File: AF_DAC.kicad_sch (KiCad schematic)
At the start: 27 parts, among them J9 3.5mm_Jack, U12 PAM8908, U4 CJC4334H

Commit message: Fixed a lot more mistakes...
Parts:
- TP8, TP9: footprint TP_Label:TestPoint_THTPad_D2.0mm_Drill1.0mm -> TestPoint:TestPoint_THTPad_D2.5mm_Drill1.2mm
- U12: Price (none) -> $0.38
- U4: Price (none) -> $0.30
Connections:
- net +3.3V renamed +3V3
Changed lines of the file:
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@@
 			)
 		)
-		(property "Footprint" "TP_Label:TestPoint_THTPad_D2.0mm_Drill1.0mm"
+		(property "Footprint" "TestPoint:TestPoint_THTPad_D2.5mm_Drill1.2mm"
 			(at 212.09 96.52 0)
 			(hide yes)
@@
 			)
 		)
+		(property "Price" "$0.38"
+			(at 166.37 88.9 0)
+			(hide yes)
+			(show_name no)
+			(do_not_autoplace no)
+			(effects
+				(font
+					(size 1.27 1.27)
+				)
+			)
+		)
 		(pin "2"
 		)
@@
 	)
 	(symbol
+		(lib_id "power:+3V3")
+		(at 72.39 53.34 0)
+		(unit 1)
+		(body_style 1)
+		(exclude_from_sim no)
+		(in_bom yes)
+		(on_board yes)
+		(in_pos_files yes)
+		(dnp no)
+		(property "Reference" "#PWR0220"
+			(at 72.39 57.15 0)
+			(hide yes)
+			(show_name no)
+			(do_not_autoplace no)
+			(effects
+				(font
+					(size 1.27 1.27)
+				)
+			)
+		)
+		(property "Value" "+3V3"
+			(at 72.771 48.9458 0)
+			(show_name no)
+			(do_not_autoplace no)
+			(effects
+				(font
+					(size 1.27 1.27)
+				)
+			)
+		)
+		(property "Footprint" ""
+			(at 72.39 53.34 0)
+			(hide yes)
+			(show_name no)
+			(do_not_autoplace no)
+			(effects
+				(font
+					(size 1.27 1.27)
+				)
+			)
+		)
+		(property "Datasheet" ""
+			(at 72.39 53.34 0)
+			(hide yes)
+			(show_name no)
+			(do_not_autoplace no)
+			(effects
+				(font
+					(size 1.27 1.27)
+				)
+			)
+		)
+		(property "Description" ""
+			(at 72.39 53.34 0)
+			(hide yes)
+			(show_name no)
+			(do_not_autoplace no)
+			(effects
+				(font
+					(size 1.27 1.27)
+				)
+			)
+		)
+		(pin "1"
+		)
+		(instances
+			(project "DDC_SDR"
+				(path "/7dfef218-ca21-47b0-a8d3-67c7d55cb9d2/41fc8a82-80f7-4b0c-8115-38fd99a62892"
+					(reference "#PWR0220")
+					(unit 1)
+				)
+			)
+		)
+	)
+	(symbol
 		(lib_id "power:GNDA")
 		(at 72.39 102.87 0)
@@
 			)
 		)
-		(property "Footprint" "TP_Label:TestPoint_THTPad_D2.0mm_Drill1.0mm"
+		(property "Footprint" "TestPoint:TestPoint_THTPad_D2.5mm_Drill1.2mm"
 			(at 222.25 86.36 0)
 			(hide yes)
@@
 			)
 		)
+		(property "Price" "$0.30"
+			(at 71.12 87.63 0)
+			(hide yes)
+			(show_name no)
+			(do_not_autoplace no)
+			(effects
+				(font
+					(size 1.27 1.27)
+				)
+			)
+		)
 		(pin "2"
 		)
@@
 					(unit 1)
 				)
-			)
-		)
-	)
-	(symbol
-		(lib_name "+3.3V_1")
-		(lib_id "power:+3.3V")
-		(at 72.39 53.34 0)
-		(mirror y)
-		(unit 1)
-		(body_style 1)
-		(exclude_from_sim no)
-		(in_bom yes)
-		(on_board yes)
-		(in_pos_files yes)
-		(dnp no)
-		(fields_autoplaced yes)
-		(property "Reference" "#PWR072"
-			(at 72.39 57.15 0)
-			(hide yes)
-			(show_name no)
-			(do_not_autoplace no)
-			(effects
-				(font
-					(size 1.27 1.27)
-				)
-			)
-		)
-		(property "Value" "+3.3V"
-			(at 72.39 48.26 0)
-			(show_name no)
-			(do_not_autoplace no)
-			(effects
-				(font
-					(size 1.27 1.27)
-				)
-			)
-		)
-		(property "Footprint" ""
-			(at 72.39 53.34 0)
-			(hide yes)
-			(show_name no)
-			(do_not_autoplace no)
-			(effects
-				(font
-					(size 1.27 1.27)
-				)
-			)
-		)
-		(property "Datasheet" ""
-			(at 72.39 53.34 0)
-			(hide yes)
-			(show_name no)
-			(do_not_autoplace no)
-			(effects
-				(font
-					(size 1.27 1.27)
-				)
-			)
-		)
-		(property "Description" "Power symbol creates a global label with name \"+3.3V\""
-			(at 72.39 53.34 0)
-			(hide yes)
-			(show_name no)
-			(do_not_autoplace no)
-			(effects
-				(font
-					(size 1.27 1.27)
-				)
-			)
-		)
-		(pin "1"
-		)
-		(instances
-			(project "DDC_SDR"
-				(path "/7dfef218-ca21-47b0-a8d3-67c7d55cb9d2/41fc8a82-80f7-4b0c-8115-38fd99a62892"
-					(reference "#PWR072")
-					(unit 1)
-				)

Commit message: Starting to place components
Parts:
- C12, C50: footprint PCM_JLCPCB:C_0805 -> PCM_JLCPCB:C_0402; symbol PCM_JLCPCB-Capacitors:0805,100nF -> PCM_JLCPCB-Capacitors:0402,100nF,(2); LCSC C28233 -> C307331; Manufacturer (none) -> Samsung Electro-Mechanics; Part CL21B104KCFNNNE -> CL05B104KB54PNC; Price 0.009USD -> 0.008USD; Stock 1168020 -> 8389599; Voltage Rated 100V -> 50V
- C26, C57: footprint PCM_JLCPCB:C_0805 -> PCM_JLCPCB:C_0603; symbol PCM_JLCPCB-Capacitors:0805,1uF -> PCM_JLCPCB-Capacitors:0603,1uF; LCSC C28323 -> C15849; Part CL21B105KBFNNNE -> CL10A105KB8NNNC; Price 0.012USD -> 0.008USD; Stock 4334256 -> 11535980; Temperature Coefficient X7R -> X5R
- C45: footprint PCM_JLCPCB:C_CASE-A-3216-18(mm) -> PCM_JLCPCB:C_0805; symbol PCM_JLCPCB-Capacitors:CASE-A-3216-18(mm),10uF -> PCM_JLCPCB-Capacitors:0805,10uF,(2); Attrition Qty 2 -> 4; Category Capacitors,Tantalum Capacitors -> Capacitors,Multilayer Ceramic Capacitors MLCC - SMD/SMT; LCSC C7171 -> C440198; Manufacturer (none) -> Murata Electronics; Part TAJA106K016RNJ -> GRM21BR61H106KE43L; Price 0.133USD -> 0.066USD; Stock 887054 -> 1422246; Temperature Coefficient (none) -> X5R; Voltage Rated (none) -> 50V
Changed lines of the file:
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@@
 	)
 	(symbol
-		(lib_id "PCM_JLCPCB-Capacitors:0805,1uF")
+		(lib_id "PCM_JLCPCB-Capacitors:0603,1uF")
 		(at 200.66 107.95 0)
 		(unit 1)
@@
 			)
 		)
-		(property "Footprint" "PCM_JLCPCB:C_0805"
+		(property "Footprint" "PCM_JLCPCB:C_0603"
 			(at 198.882 107.95 90)
 			(hide yes)
@@
 			)
 		)
-		(property "Datasheet" "https://www.lcsc.com/datasheet/lcsc_datasheet_2304140030_Samsung-Electro-Mechanics-CL21B105KBFNNNE_C28323.pdf"
+		(property "Datasheet" "https://www.lcsc.com/datasheet/lcsc_datasheet_2304140030_Samsung-Electro-Mechanics-CL10A105KB8NNNC_C15849.pdf"
 			(at 200.66 107.95 0)
 			(hide yes)
@@
 			)
 		)
-		(property "Description" "50V 1uF X7R ±10% 0805 Multilayer Ceramic Capacitors MLCC - SMD/SMT ROHS"
+		(property "Description" "50V 1uF X5R ±10% 0603 Multilayer Ceramic Capacitors MLCC - SMD/SMT ROHS"
 			(at 200.66 107.95 0)
 			(hide yes)
@@
 			)
 		)
-		(property "LCSC" "C28323"
+		(property "LCSC" "C15849"
 			(at 200.66 107.95 0)
 			(hide yes)
@@
 			)
 		)
-		(property "Stock" "4334256"
+		(property "Stock" "11535980"
 			(at 200.66 107.95 0)
 			(hide yes)
@@
 			)
 		)
-		(property "Price" "0.012USD"
+		(property "Price" "0.008USD"
 			(at 200.66 107.95 0)
 			(hide yes)
@@
 			)
 		)
-		(property "Part" "CL21B105KBFNNNE"
+		(property "Part" "CL10A105KB8NNNC"
 			(at 200.66 107.95 0)
 			(hide yes)
@@
 			)
 		)
-		(property "Temperature Coefficient" "X7R"
+		(property "Temperature Coefficient" "X5R"
 			(at 200.66 107.95 0)
 			(hide yes)
@@
 	)
 	(symbol
-		(lib_id "PCM_JLCPCB-Capacitors:0805,1uF")
+		(lib_id "PCM_JLCPCB-Capacitors:0603,1uF")
 		(at 185.42 107.95 0)
 		(unit 1)
@@
 			)
 		)
-		(property "Footprint" "PCM_JLCPCB:C_0805"
+		(property "Footprint" "PCM_JLCPCB:C_0603"
 			(at 183.642 107.95 90)
 			(hide yes)
@@
 			)
 		)
-		(property "Datasheet" "https://www.lcsc.com/datasheet/lcsc_datasheet_2304140030_Samsung-Electro-Mechanics-CL21B105KBFNNNE_C28323.pdf"
+		(property "Datasheet" "https://www.lcsc.com/datasheet/lcsc_datasheet_2304140030_Samsung-Electro-Mechanics-CL10A105KB8NNNC_C15849.pdf"
 			(at 185.42 107.95 0)
 			(hide yes)
@@
 			)
 		)
-		(property "Description" "50V 1uF X7R ±10% 0805 Multilayer Ceramic Capacitors MLCC - SMD/SMT ROHS"
+		(property "Description" "50V 1uF X5R ±10% 0603 Multilayer Ceramic Capacitors MLCC - SMD/SMT ROHS"
 			(at 185.42 107.95 0)
 			(hide yes)
@@
 			)
 		)
-		(property "LCSC" "C28323"
+		(property "LCSC" "C15849"
 			(at 185.42 107.95 0)
 			(hide yes)
@@
 			)
 		)
-		(property "Stock" "4334256"
+		(property "Stock" "11535980"
 			(at 185.42 107.95 0)
 			(hide yes)
@@
 			)
 		)
-		(property "Price" "0.012USD"
+		(property "Price" "0.008USD"
 			(at 185.42 107.95 0)
 			(hide yes)
@@
 			)
 		)
-		(property "Part" "CL21B105KBFNNNE"
+		(property "Part" "CL10A105KB8NNNC"
 			(at 185.42 107.95 0)
 			(hide yes)
@@
 			)
 		)
-		(property "Temperature Coefficient" "X7R"
+		(property "Temperature Coefficient" "X5R"
 			(at 185.42 107.95 0)
 			(hide yes)
@@
 	)
 	(symbol
-		(lib_id "PCM_JLCPCB-Capacitors:0805,100nF")
+		(lib_id "PCM_JLCPCB-Capacitors:0402,100nF,(2)")
 		(at 226.06 101.6 180)
 		(unit 1)
@@
 			)
 		)
-		(property "Footprint" "PCM_JLCPCB:C_0805"
+		(property "Footprint" "PCM_JLCPCB:C_0402"
 			(at 227.838 101.6 90)
 			(hide yes)
@@
 			)
 		)
-		(property "Datasheet" "https://www.lcsc.com/datasheet/lcsc_datasheet_2304140030_Samsung-Electro-Mechanics-CL21B104KCFNNNE_C28233.pdf"
+		(property "Datasheet" "https://www.lcsc.com/datasheet/lcsc_datasheet_2304140030_Samsung-Electro-Mechanics-CL05B104KB54PNC_C307331.pdf"
 			(at 226.06 101.6 0)
 			(hide yes)
@@
 			)
 		)
-		(property "Description" "100V 100nF X7R ±10% 0805 Multilayer Ceramic Capacitors MLCC - SMD/SMT ROHS"
+		(property "Description" "50V 100nF X7R ±10% 0402 Multilayer Ceramic Capacitors MLCC - SMD/SMT ROHS"
 			(at 226.06 101.6 0)
 			(hide yes)
@@
 			)
 		)
-		(property "LCSC" "C28233"
+		(property "LCSC" "C307331"
 			(at 226.06 101.6 0)
 			(hide yes)
@@
 			)
 		)
-		(property "Stock" "1168020"
+		(property "Stock" "8389599"
 			(at 226.06 101.6 0)
 			(hide yes)
@@
 			)
 		)
-		(property "Price" "0.009USD"
+		(property "Price" "0.008USD"
 			(at 226.06 101.6 0)
 			(hide yes)
@@
 			)
 		)
-		(property "Part" "CL21B104KCFNNNE"
+		(property "Part" "CL05B104KB54PNC"
 			(at 226.06 101.6 0)
 			(hide yes)
@@
 			)
 		)
-		(property "Voltage Rated" "100V"
-			(at 220.218 104.394 0)
+		(property "Voltage Rated" "50V"
+			(at 224.028 99.5538 0)
 			(show_name no)
 			(do_not_autoplace no)
@@
 					(size 0.8 0.8)
 				)
-				(justify right)
+				(justify left)
 			)
 		)
@@
 			)
 		)
+		(property "Manufacturer" "Samsung Electro-Mechanics"
+			(at 226.06 101.6 0)
+			(hide yes)
+			(show_name no)
+			(do_not_autoplace no)
+			(effects
+				(font
+					(size 1.27 1.27)
+				)
+			)
+		)
 		(pin "2"
 		)
@@
 	)
 	(symbol
-		(lib_id "PCM_JLCPCB-Capacitors:0805,100nF")
+		(lib_id "PCM_JLCPCB-Capacitors:0402,100nF,(2)")
 		(at 83.82 64.77 0)
 		(unit 1)
@@
 			)
 		)
-		(property "Footprint" "PCM_JLCPCB:C_0805"
+		(property "Footprint" "PCM_JLCPCB:C_0402"
 			(at 82.042 64.77 90)
 			(hide yes)
@@
 			)
 		)
-		(property "Datasheet" "https://www.lcsc.com/datasheet/lcsc_datasheet_2304140030_Samsung-Electro-Mechanics-CL21B104KCFNNNE_C28233.pdf"
+		(property "Datasheet" "https://www.lcsc.com/datasheet/lcsc_datasheet_2304140030_Samsung-Electro-Mechanics-CL05B104KB54PNC_C307331.pdf"
 			(at 83.82 64.77 0)
 			(hide yes)
@@
 			)
 		)
-		(property "Description" "100V 100nF X7R ±10% 0805 Multilayer Ceramic Capacitors MLCC - SMD/SMT ROHS"
+		(property "Description" "50V 100nF X7R ±10% 0402 Multilayer Ceramic Capacitors MLCC - SMD/SMT ROHS"
 			(at 83.82 64.77 0)
 			(hide yes)
@@
 			)
 		)
-		(property "LCSC" "C28233"
+		(property "LCSC" "C307331"
 			(at 83.82 64.77 0)
 			(hide yes)
@@
 			)
 		)
-		(property "Stock" "1168020"
+		(property "Stock" "8389599"
 			(at 83.82 64.77 0)
 			(hide yes)
@@
 			)
 		)
-		(property "Price" "0.009USD"
+		(property "Price" "0.008USD"
 			(at 83.82 64.77 0)
 			(hide yes)
@@
 			)
 		)
-		(property "Part" "CL21B104KCFNNNE"
+		(property "Part" "CL05B104KB54PNC"
 			(at 83.82 64.77 0)
 			(hide yes)
@@
 			)
 		)
-		(property "Voltage Rated" "100V"
+		(property "Voltage Rated" "50V"
 			(at 86.36 67.31 0)
 			(show_name no)
@@
 			)
 		)
+		(property "Manufacturer" "Samsung Electro-Mechanics"
+			(at 83.82 64.77 0)
+			(hide yes)
+			(show_name no)
+			(do_not_autoplace no)
+			(effects
+				(font
+					(size 1.27 1.27)
+				)
+			)
+		)
 		(pin "1"
 		)
@@
 	)
 	(symbol
-		(lib_id "PCM_JLCPCB-Capacitors:CASE-A-3216-18(mm),10uF")
+		(lib_id "PCM_JLCPCB-Capacitors:0805,10uF,(2)")
 		(at 92.71 64.77 0)
 		(unit 1)
@@
 			)
 		)
-		(property "Footprint" "PCM_JLCPCB:C_CASE-A-3216-18(mm)"
+		(property "Footprint" "PCM_JLCPCB:C_0805"
 			(at 90.932 64.77 90)
 			(hide yes)
@@
 			)
 		)
-		(property "Datasheet" "https://www.lcsc.com/datasheet/lcsc_datasheet_2304140030_Kyocera-AVX-TAJA106K016RNJ_C7171.pdf"
+		(property "Datasheet" "https://www.lcsc.com/datasheet/lcsc_datasheet_2411041759_Murata-Electronics-GRM21BR61H106KE43L_C440198.pdf"
 			(at 92.71 64.77 0)
 			(hide yes)
@@
 			)
 		)
-		(property "Description" "10uF 16V 3Ω@100kHz ±10% CASE-A-3216-18(mm) Tantalum Capacitors ROHS"
+		(property "Description" "50V 10uF X5R ±10% 0805 Multilayer Ceramic Capacitors MLCC - SMD/SMT ROHS"
 			(at 92.71 64.77 0)
 			(hide yes)
@@
 			)
 		)
-		(property "LCSC" "C7171"
+		(property "LCSC" "C440198"
 			(at 92.71 64.77 0)
 			(hide yes)
@@
 			)
 		)
-		(property "Stock" "887054"
+		(property "Stock" "1422246"
 			(at 92.71 64.77 0)
 			(hide yes)
@@
 			)
 		)
-		(property "Price" "0.133USD"
+		(property "Price" "0.066USD"
 			(at 92.71 64.77 0)
 			(hide yes)
@@
 			)
 		)
-		(property "Attrition Qty" "2"
+		(property "Attrition Qty" "4"
 			(at 92.71 64.77 0)
 			(hide yes)
@@
 			)
 		)
-		(property "Category" "Capacitors,Tantalum Capacitors"
+		(property "Category" "Capacitors,Multilayer Ceramic Capacitors MLCC - SMD/SMT"
 			(at 92.71 64.77 0)
 			(hide yes)
@@
 			)
 		)
-		(property "Part" "TAJA106K016RNJ"
+		(property "Part" "GRM21BR61H106KE43L"
 			(at 92.71 64.77 0)
 			(hide yes)
@@
 		(property "Rated Voltage" "16V"
 			(at 96.266 67.564 0)
+			(hide yes)
+			(show_name no)
+			(do_not_autoplace no)
+			(effects
+				(font
+					(size 0.8 0.8)
+				)
+			)
+		)
+		(property "Manufacturer" "Murata Electronics"
+			(at 92.71 64.77 0)
+			(hide yes)
+			(show_name no)
+			(do_not_autoplace no)
+			(effects
+				(font
+					(size 1.27 1.27)
+				)
+			)
+		)
+		(property "Voltage Rated" "50V"
+			(at 94.742 66.8162 0)
 			(show_name no)
 			(do_not_autoplace no)
@@
 					(size 0.8 0.8)
 				)
+				(justify left)
+			)
+		)
+		(property "Temperature Coefficient" "X5R"
+			(at 92.71 64.77 0)
+			(hide yes)
+			(show_name no)
+			(do_not_autoplace no)
+			(effects
+				(font
+					(size 1.27 1.27)
+				)
 			)

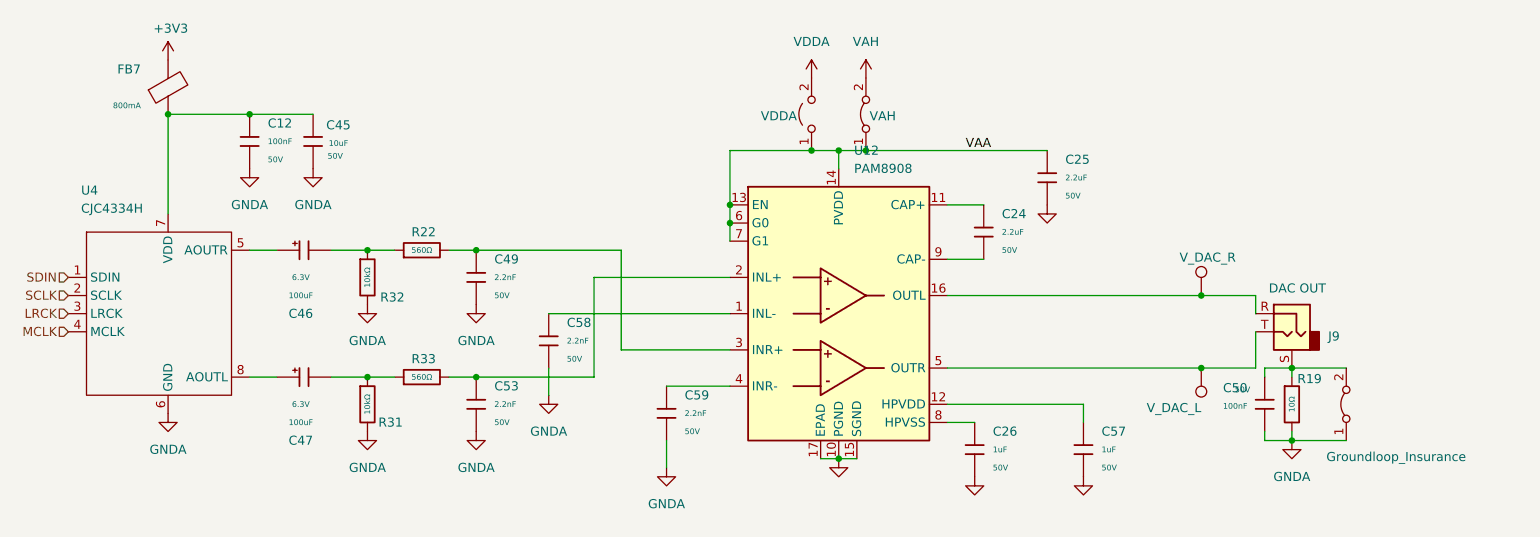
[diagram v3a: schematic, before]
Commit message: AF DAC Some VDDA Placed
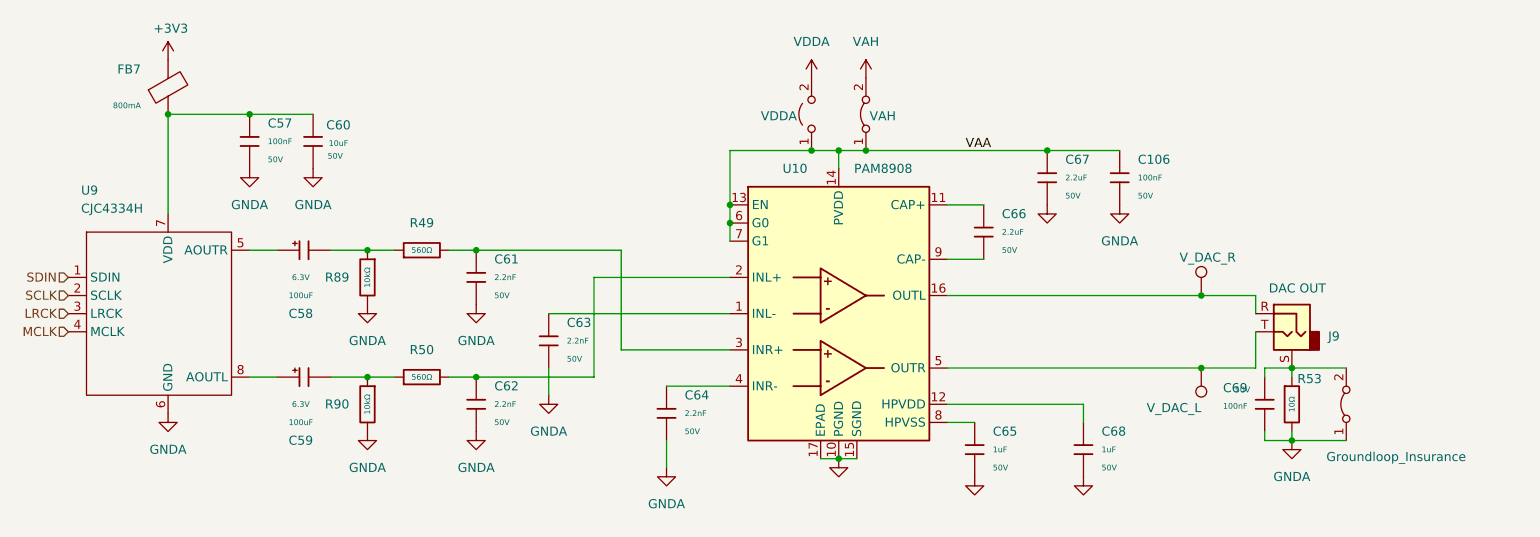
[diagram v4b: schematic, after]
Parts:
- removed R22, R33: 560Ω, PCM_JLCPCB:R_0805, symbol PCM_JLCPCB-Resistors:0805,560Ω
- removed R31, R32: 10kΩ, PCM_JLCPCB:R_0805, symbol PCM_JLCPCB-Resistors:0805,10kΩ
- added C106: 100nF, PCM_JLCPCB:C_0402, symbol PCM_JLCPCB-Capacitors:0402,100nF,(2)
- added R49, R50: 560Ω, PCM_JLCPCB:R_0603, symbol PCM_JLCPCB-Resistors:0603,560Ω
- added R89, R90: 10kΩ, PCM_JLCPCB:R_0402, symbol PCM_JLCPCB-Resistors:0402,10kΩ
- renumbered C12 to C57, C46 to C58, C47 to C59, C45 to C60, C49 to C61, C53 to C62, C58 to C63, C59 to C64, C26 to C65, C24 to C66, C25 to C67, C57 to C68, C50 to C69, JP3 to JP6, R19 to R53, TP8 to TP7, TP9 to TP8, U12 to U10, U4 to U9, e2 to e3, e3 to e4
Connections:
- net GNDA: now also C106.2, R89.2, R90.2
- net VAA: now also C106.1
- net at C62.1, U10.2 (INL+): now also R50.2
- net at C58.2: now also R49.1, R89.1
- net at C61.1, U10.3 (INR+): now also R49.2
- net at C59.2: now also R50.1, R90.1

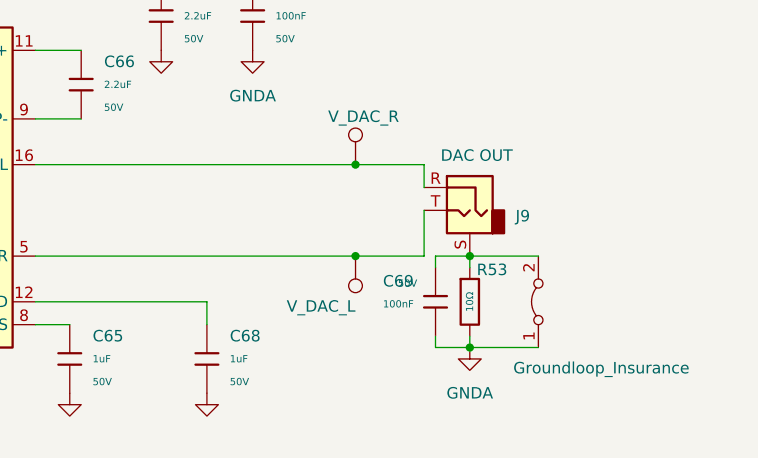
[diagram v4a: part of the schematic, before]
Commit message: SMA/LogicAnalyzer and VDDA placed
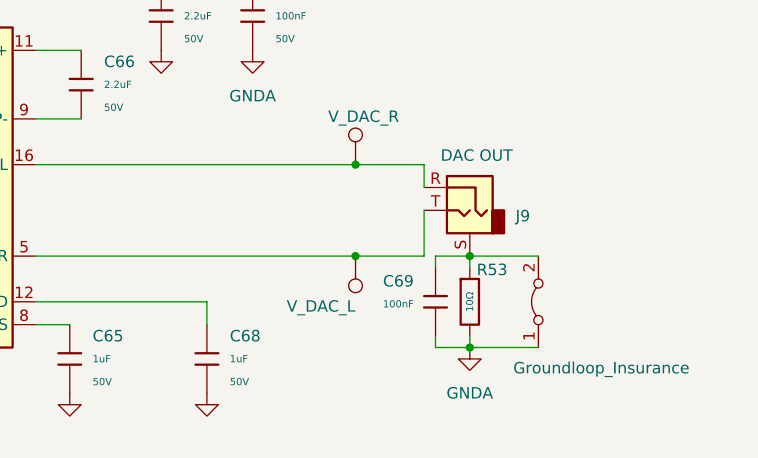
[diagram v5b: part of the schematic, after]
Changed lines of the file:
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@@
 		(property "Voltage Rated" "50V"
 			(at 224.028 99.5538 0)
+			(hide yes)
 			(show_name no)
 			(do_not_autoplace no)

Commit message: Fixed schematic errors, all placed
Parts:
- U9: symbol CJC4334H:CJC4334H -> CJC5340:CJC4334H
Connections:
- net GNDA: no longer C106.2, C57.2, C60.2, C62.2, C63.2, C64.2, C65.2, C68.2, C69.1, R53.2, R90.2, U9.6 (GND), e4.1 (A)
- net VAH renamed +4.7V
- new net GND: C106.2, C57.2, C60.2, C62.2, C63.2, C64.2, C65.2, C68.2, C69.1, R53.2, R90.2, U9.6 (GND), e4.1 (A)
